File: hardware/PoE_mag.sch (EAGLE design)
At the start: 124 parts, among them IC1 LD1117V33, IC10 74LVC1T45SOT23-HAND, IC11 74LVC1T45SOT23-HAND, IC12 PCA9517A, IC2 LD1117V33, IC3 DS1338, IC4 ATMEGA1284, IC5 TSR 1-2450, IC6 LM61, IC7 MCP2200, IC8 74LVC1T45SOT23-HAND, IC9 74LVC1T45SOT23-HAND, Q1 BSS138, Q2 BUK98150-55A, X1 PWR, X2 JTAG, X3 USB, X4 MICRO-SD-SOCKETHIROSE-DM3D, X5 CONN-SMATHD, X6 UFL, X7 22-23-2021, X8 RJ45, X9 RJ11, Y1 32k768, Y2 16MHz, Y3 12MHz

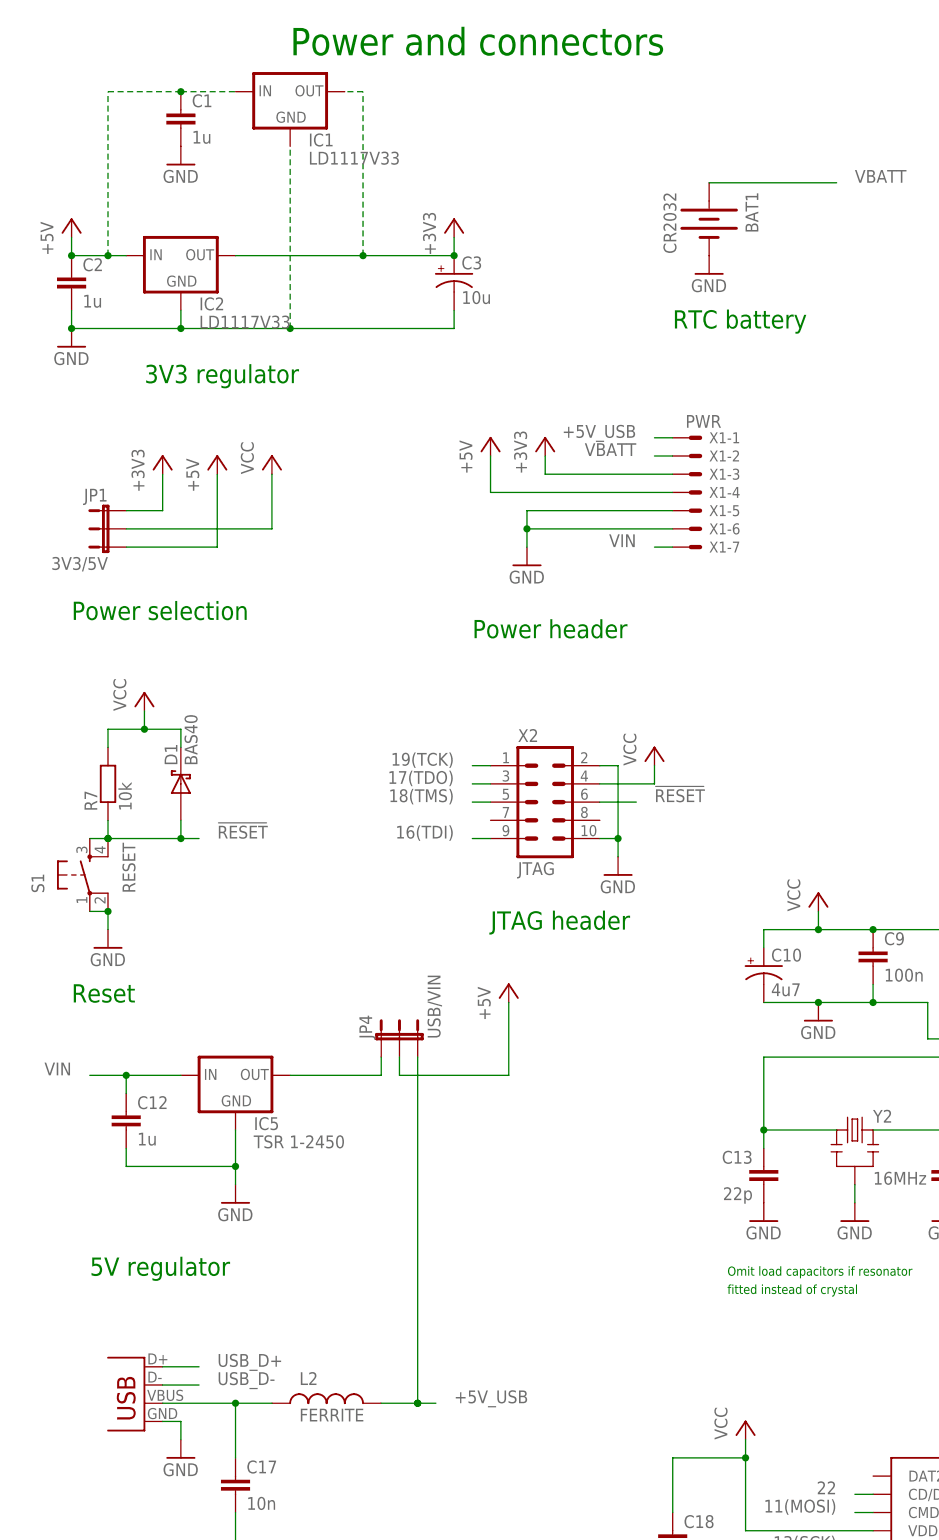
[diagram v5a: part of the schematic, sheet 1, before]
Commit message: Improve decoupling for voltage regulators
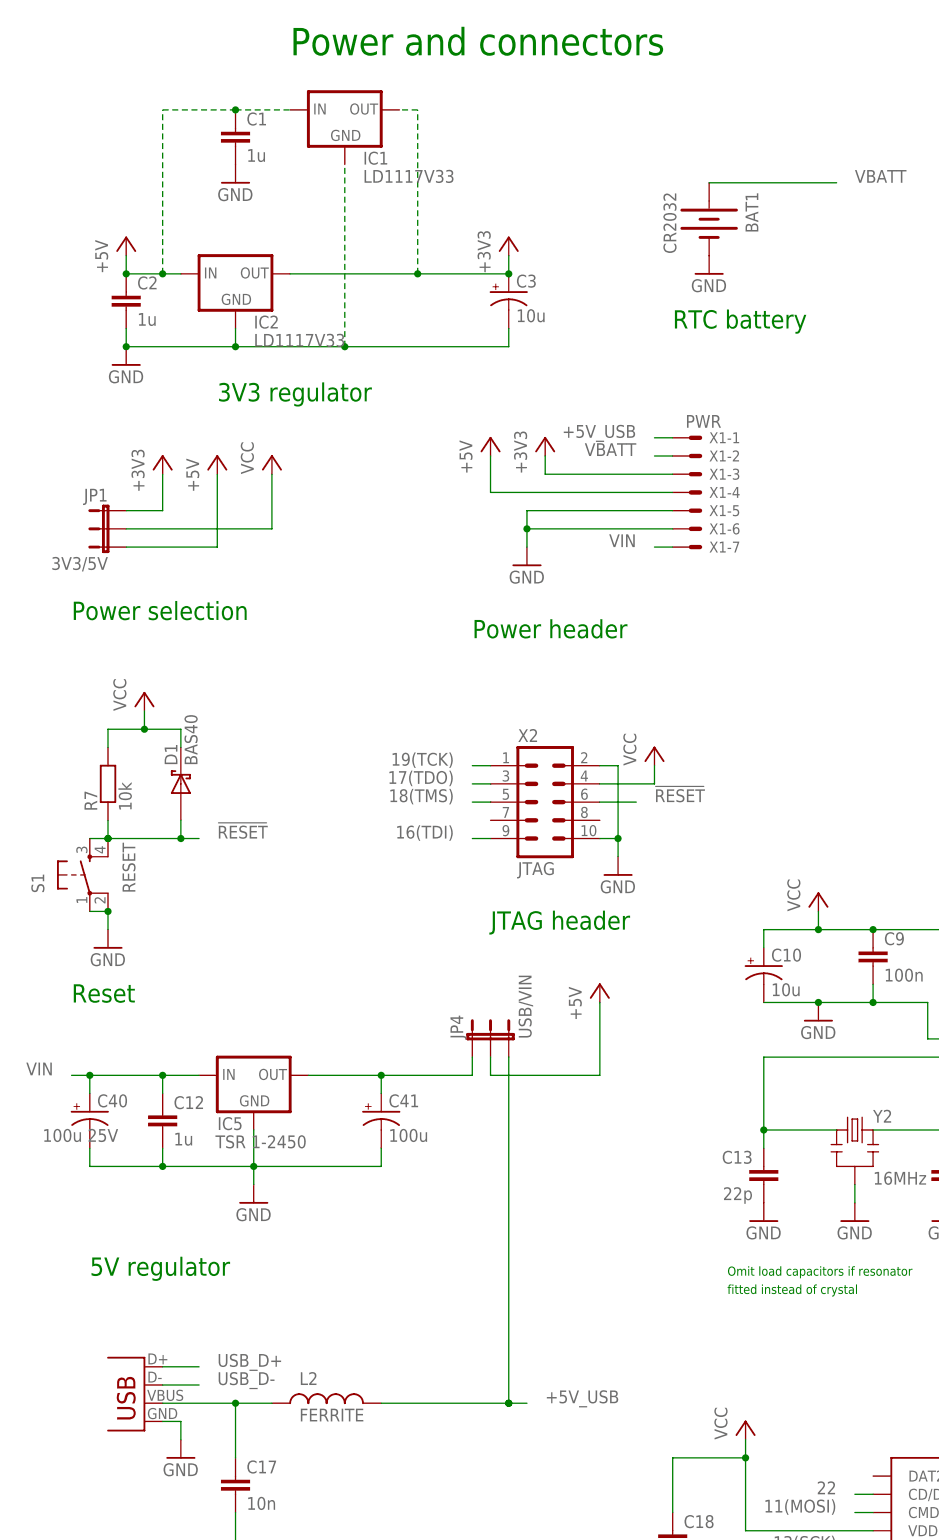
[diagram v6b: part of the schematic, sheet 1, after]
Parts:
- added C40: 100u 25V, SteveMarple:CAP_POL
- added C41: 100u, SteveMarple:CAP_POL100UF-16V-100MIL
- C10: value 4u7 -> 10u; device SparkFun:CAP_POLPTH2 -> SteveMarple:CAP_POLPTH2
- C37: value 4u7 -> 10u
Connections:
- net GND: now also C40.-, C41.-
- net N$14: now also C41.+
- net VIN: now also C40.+
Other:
- moved on the sheet: C1, C12, C2, C3, IC1, IC2, IC5, JP4

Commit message: Renumber components
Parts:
- C12: value 1u -> 100u 25V; device SteveMarple:C-EU1206-HAND -> SteveMarple:CAP_POL
- C13: value 22p -> 1u; device SteveMarple:C-EU0805-HAND -> SteveMarple:C-EU1206-HAND; OPTION Do not fit for ceramic resonator -> (none)
- C14: value 22p -> 100u; device SteveMarple:C-EU0805-HAND -> SteveMarple:CAP_POL100UF-16V-100MIL; OPTION Do not fit for ceramic resonator -> (none)
- C15, C16: value 100n -> 22p; device SteveMarple:C-EU1206-HAND -> SteveMarple:C-EU0805-HAND; OPTION (none) -> Do not fit for ceramic resonator
- C17: value 10n -> 100n
- C19: value 22p -> 10n; device SteveMarple:C-EU0805-HAND -> SteveMarple:C-EU1206-HAND
- C20, C31: value 22p -> 100n; device SteveMarple:C-EU0805-HAND -> SteveMarple:C-EU1206-HAND
- C21, C22: value 100n -> 22p; device SteveMarple:C-EU1206-HAND -> SteveMarple:C-EU0805-HAND
- C30: value 1u -> 100n
- C33, C36: value 1u -> 22p; device SteveMarple:C-EU1206-HAND -> SteveMarple:C-EU0805-HAND
- C34, C35: value 22p -> 1u; device SteveMarple:C-EU0805-HAND -> SteveMarple:C-EU1206-HAND
- C37: value 10u -> 22p; device SteveMarple:CAP_POLPTH2 -> SteveMarple:C-EU0805-HAND
- C38: value 100n -> 1u
- C39: value 100n -> 10u; device SteveMarple:C-EU1206-HAND -> SteveMarple:CAP_POLPTH2
- C40: value 100u 25V -> 100n; device SteveMarple:CAP_POL -> SteveMarple:C-EU1206-HAND
- C41: value 100u -> 100n; device SteveMarple:CAP_POL100UF-16V-100MIL -> SteveMarple:C-EU1206-HAND
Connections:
- net !RESET: now also C23.2; no longer C21.2
- net +3V3: now also C18.1, C34.1, C35.1; no longer C16.1, C26.1, C27.1
- net GND: now also C12.-, C14.-, C21.2, C34.2, C37.2, C39.-, C40.2, C41.2; no longer C12.2, C14.2, C23.2, C36.2, C37.-, C39.2, C40.-, C41.-
- net MAG_VCC: now also C41.1; no longer C39.1
- net N$1: now also C16.1; no longer C14.1
- net N$14: now also C14.+; no longer C41.+
- net N$15: now also C23.1; no longer C21.1
- net N$18: now also C21.1; no longer C19.1
- net N$2: now also C15.1; no longer C13.1
- net N$23: now also C36.2; no longer C34.2
- net N$24: now also C36.1; no longer C34.1
- net N$7: now also C22.1; no longer C20.1
- net VBUS: now also C19.1; no longer C17.1
- net VCC: now also C17.1, C20.1, C26.1, C27.1, C40.1; no longer C15.1, C18.1, C22.1, C23.1, C38.1
- net VIN: now also C12.+, C13.1; no longer C12.1, C40.+
- net V_ANT: now also C37.1, C38.1, C39.+; no longer C35.1, C36.1, C37.+
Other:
- moved on the sheet: C13, C15, C16, C17, C18, C19, C20, C21, C24, C25, C26, C27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

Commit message: Move battery holder
Move to create more room so that alternative versions can be used.
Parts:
- BAT1: device SparkFun:BATTERY20PTH -> SteveMarple:BATTERY20PTH
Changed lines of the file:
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@@
 <part name="P+6" library="supply1" deviceset="VCC" device=""/>
 <part name="P+8" library="supply1" deviceset="VCC" device=""/>
-<part name="BAT1" library="SparkFun" deviceset="BATTERY" device="20PTH" value="CR2032"/>
+<part name="BAT1" library="SteveMarple" deviceset="BATTERY" device="20PTH" value="CR2032"/>
 <part name="GND26" library="supply1" deviceset="GND" device=""/>
 <part name="X2" library="SteveMarple" deviceset="ATMEL-JTAG" device="" value="JTAG"/>
